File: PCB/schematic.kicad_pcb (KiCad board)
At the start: 2 copper layers, 76.8 x 45.2 mm, 5 parts, among them SW1 SW_Push, SW2 SW_Push, SW3 SW_Push, SW4 RotaryEncoder_Switch, U1 MOUDLE-SEEEDUINO-XIAO

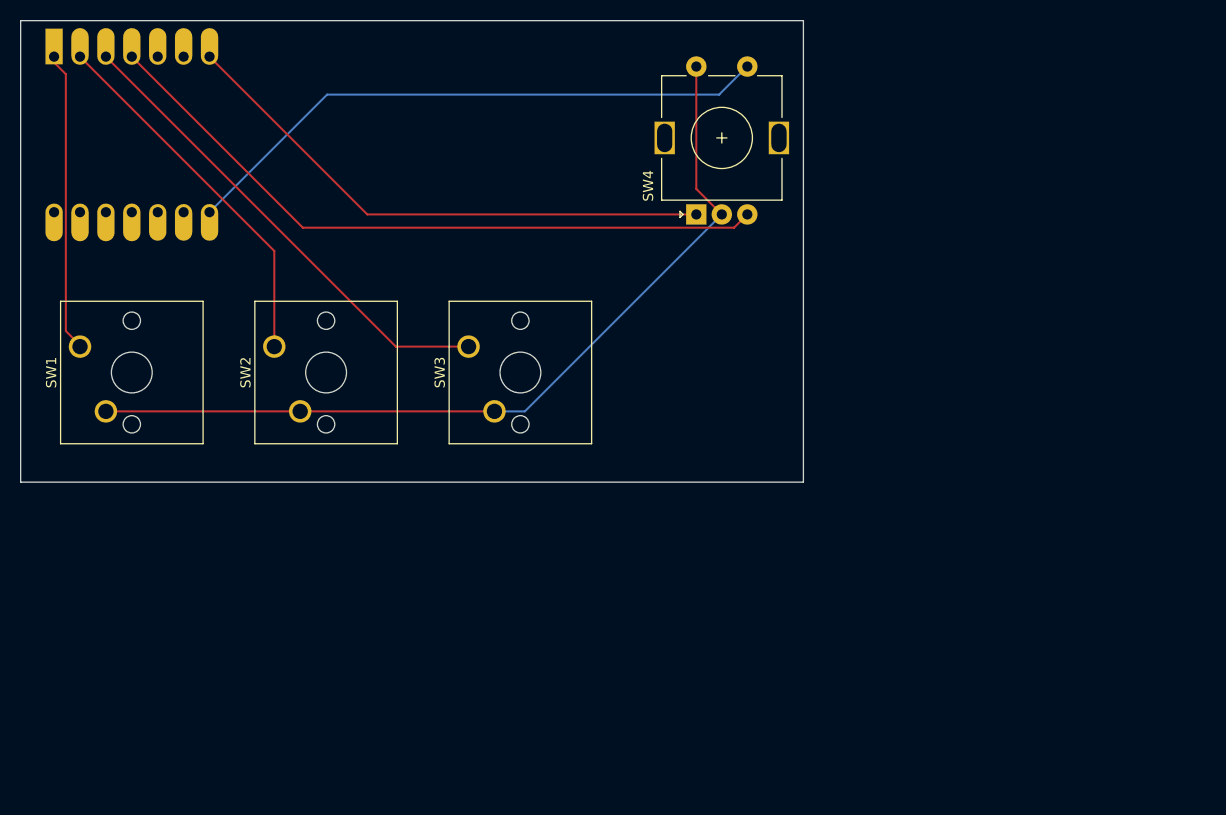
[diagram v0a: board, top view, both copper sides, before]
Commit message: Complete revamp of the 3d models due to precision mistakes repaired using 3d models of mechanical parts. Minor chnages to readme.
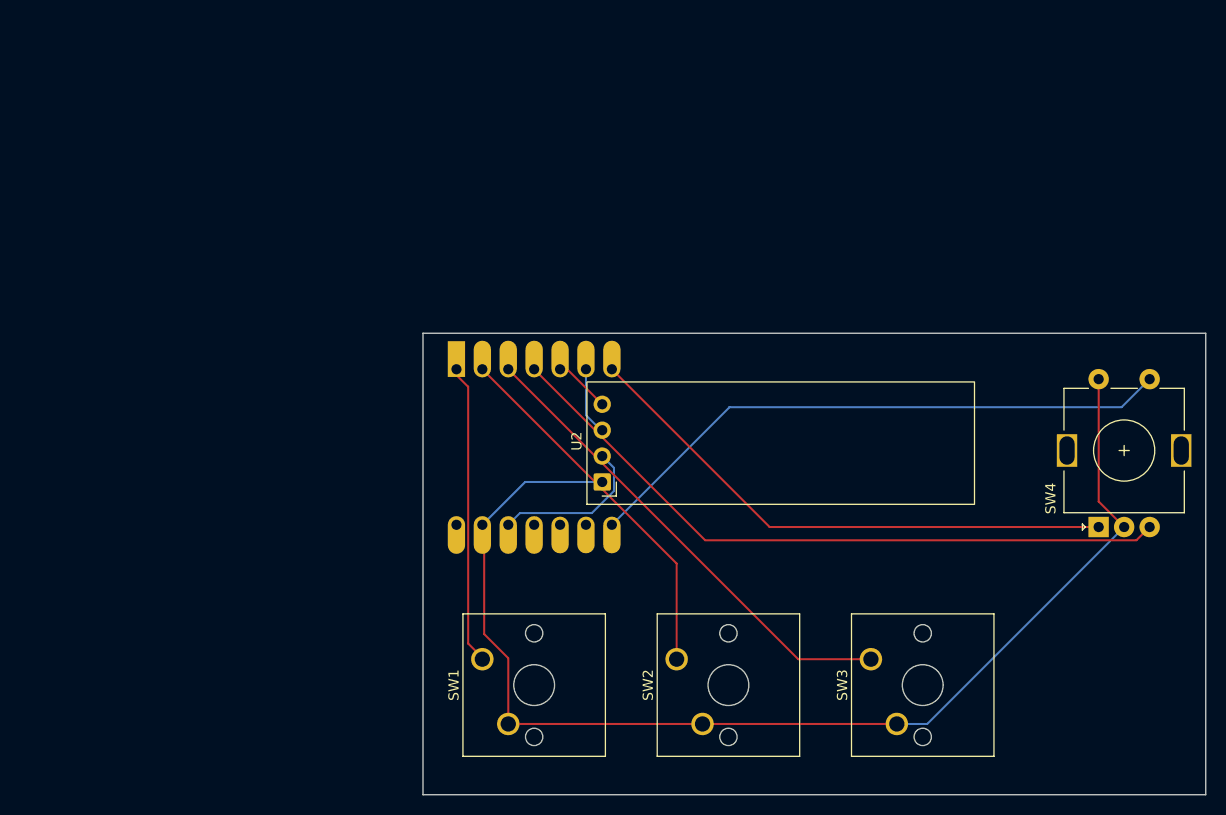
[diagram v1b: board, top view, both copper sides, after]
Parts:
- added U2: ER_OLEDM0.91_1x-I2C, Display:ER_OLEDM0.91_1x-I2C, F.Cu at (103.3, 80.7)
- moved SW3 50.0 mm to (129.6, 98.1)
- moved SW1 50.0 mm to (91.5, 98.1)
- moved U1 50.0 mm to (96.6, 77.3)
- moved SW2 50.0 mm to (110.6, 98.1)
- moved SW4 50.0 mm to (151.9, 85.2)
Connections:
- U1 pad 12: Net-(D1-VDD) -> +3.3V
- U1 pad 13: unconnected-(U1-GND-Pad13) -> GND
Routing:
- net GND: track 83.9 -> 118.3 mm
- net +3.3V: track 0.00 -> 15.6 mm
- net Net-(U1-PA9_A5_D5_SCL): track 0.00 -> 6.87 mm
- net Net-(U1-PA8_A4_D4_SDA): track 0.00 -> 5.56 mm
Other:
- board size 76.8 x 45.2 mm -> 76.7 x 45.2 mm
